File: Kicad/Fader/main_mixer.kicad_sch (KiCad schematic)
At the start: 10 parts, among them U1 OPA134, U2 OPA134

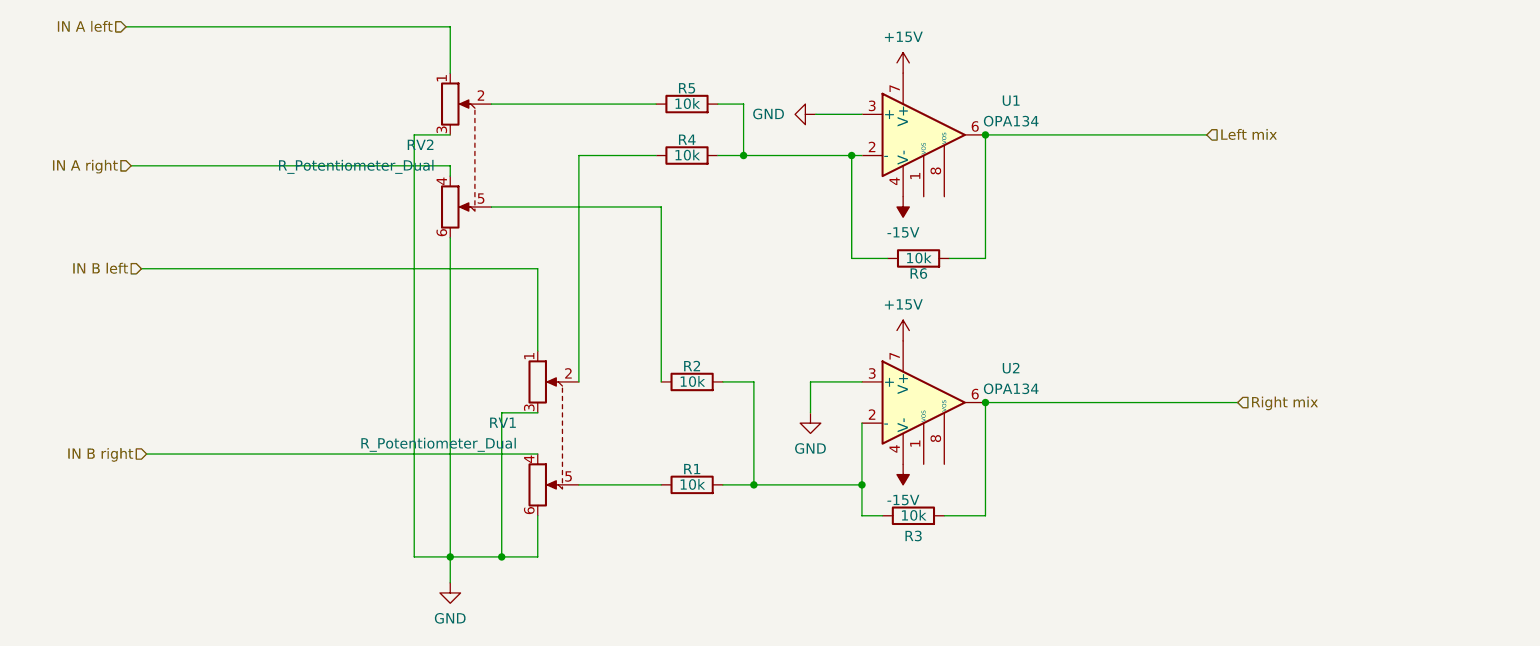
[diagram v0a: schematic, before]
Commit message: added amp and power bypass
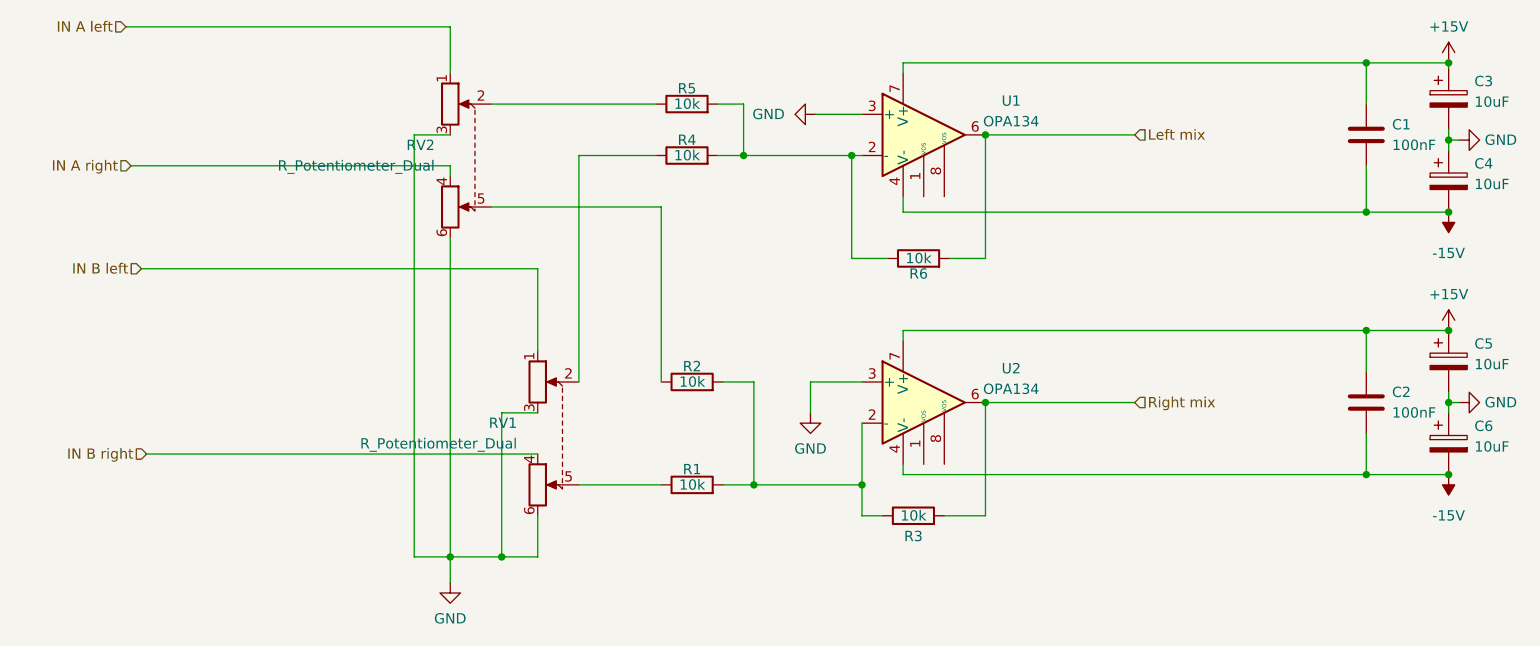
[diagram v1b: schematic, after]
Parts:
- added C1, C2: 100nF, symbol Device:C
- added C3, C4, C5, C6: 10uF, symbol Device:C_Polarized
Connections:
- net +15V: now also C1.1, C2.1, C3.1, C5.1
- net -15V: now also C1.2, C2.2, C4.2, C6.2
- net GND: now also C3.2, C4.1, C5.2, C6.1
